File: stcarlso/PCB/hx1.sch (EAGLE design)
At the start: 5 parts, among them J1 SMA_EDGE, J2 CTRL, U1 HX1

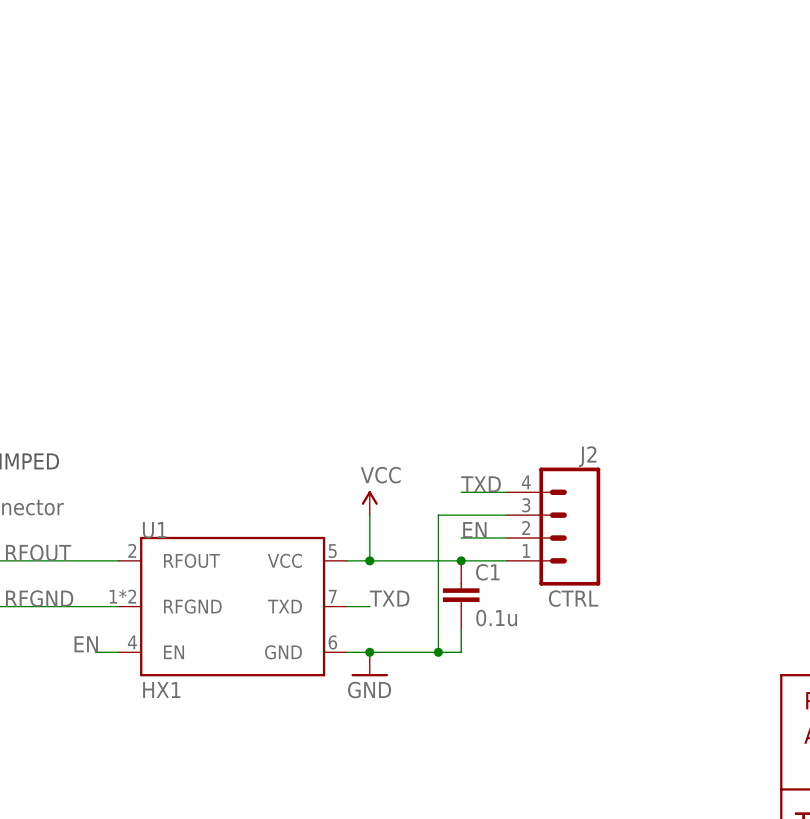
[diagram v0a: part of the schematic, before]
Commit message: Update PCB to include pads for RC filter (values TBD)
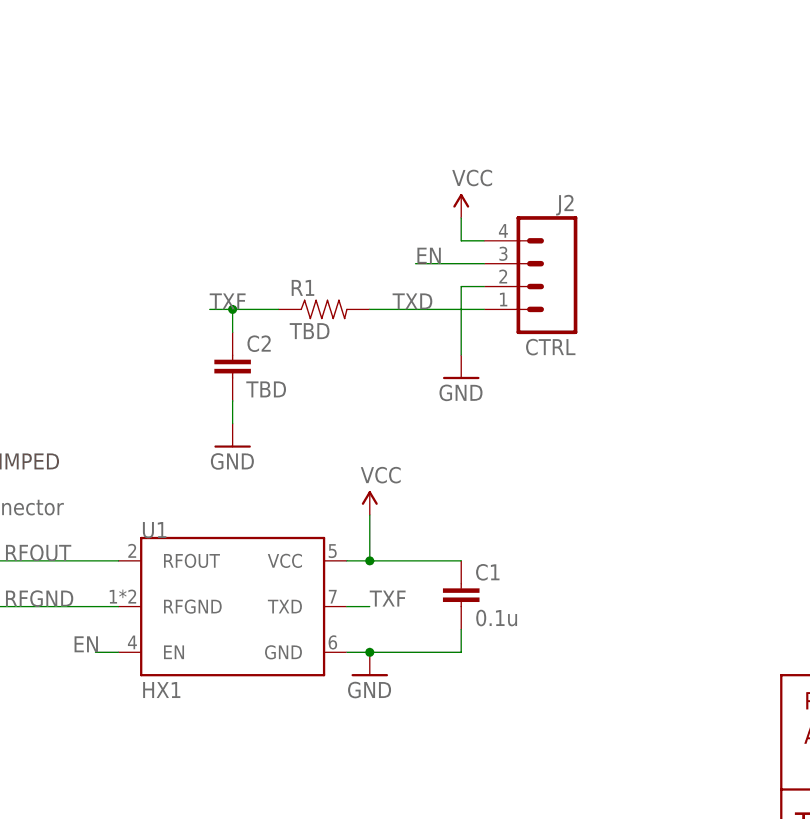
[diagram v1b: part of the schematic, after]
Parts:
- added C2: TBD, SparkFun-Passives:CAPPTH
- added R1: TBD, SparkFun-Passives:RESISTORAXIAL-0.3
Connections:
- new net TXF: C2.1, R1.1, U1.TXD
- net EN: now also J2.3; no longer J2.2
- net GND: now also C2.2, J2.2; no longer J2.3
- net TXD: now also J2.1, R1.2; no longer J2.4, U1.TXD
- net VCC: now also J2.4; no longer J2.1
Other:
- moved on the sheet: J2
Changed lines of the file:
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@@
 <part name="SUPPLY1" library="SparkFun-Aesthetics" deviceset="VCC" device=""/>
 <part name="C1" library="SparkFun-Passives" deviceset="CAP" device="PTH" value="0.1u"/>
+<part name="R1" library="SparkFun-Passives" deviceset="RESISTOR" device="AXIAL-0.3" value="TBD"/>
+<part name="C2" library="SparkFun-Passives" deviceset="CAP" device="PTH" value="TBD"/>
+<part name="GND2" library="SparkFun-Aesthetics" deviceset="GND" device=""/>
+<part name="GND3" library="SparkFun-Aesthetics" deviceset="GND" device=""/>
+<part name="SUPPLY2" library="SparkFun-Aesthetics" deviceset="VCC" device=""/>
 </parts>
 <sheets>
@@
 <instance part="FRAME1" gate="G$1" x="0" y="0"/>
 <instance part="FRAME1" gate="V" x="147.32" y="0"/>
-<instance part="J2" gate="G$1" x="121.92" y="50.8" rot="MR0"/>
+<instance part="J2" gate="G$1" x="119.38" y="78.74" rot="MR0"/>
 <instance part="GND1" gate="1" x="101.6" y="35.56"/>
 <instance part="SUPPLY1" gate="G$1" x="101.6" y="53.34"/>
 <instance part="C1" gate="G$1" x="111.76" y="43.18"/>
+<instance part="R1" gate="G$1" x="96.52" y="76.2"/>
+<instance part="C2" gate="G$1" x="86.36" y="68.58"/>
+<instance part="GND2" gate="1" x="86.36" y="60.96"/>
+<instance part="GND3" gate="1" x="111.76" y="68.58"/>
+<instance part="SUPPLY2" gate="G$1" x="111.76" y="86.36"/>
 </instances>
 <busses>
@@
 </segment>
 <segment>
-<pinref part="J2" gate="G$1" pin="2"/>
-<wire x1="111.76" y1="50.8" x2="116.84" y2="50.8" width="0.1524" layer="91"/>
-<label x="111.76" y="50.8" size="1.778" layer="95"/>
+<pinref part="J2" gate="G$1" pin="3"/>
+<wire x1="114.3" y1="81.28" x2="106.68" y2="81.28" width="0.1524" layer="91"/>
+<label x="106.68" y="81.28" size="1.778" layer="95"/>
 </segment>
 </net>
@@
 <wire x1="101.6" y1="48.26" x2="99.06" y2="48.26" width="0.1524" layer="91"/>
 <wire x1="101.6" y1="53.34" x2="101.6" y2="48.26" width="0.1524" layer="91"/>
-<pinref part="J2" gate="G$1" pin="1"/>
 <wire x1="101.6" y1="48.26" x2="111.76" y2="48.26" width="0.1524" layer="91"/>
 <junction x="101.6" y="48.26"/>
 <pinref part="C1" gate="G$1" pin="1"/>
-<wire x1="111.76" y1="48.26" x2="116.84" y2="48.26" width="0.1524" layer="91"/>
-<junction x="111.76" y="48.26"/>
-</segment>
-</net>
-<net name="TXD" class="0">
-<segment>
-<pinref part="U1" gate="G$1" pin="TXD"/>
-<wire x1="101.6" y1="43.18" x2="99.06" y2="43.18" width="0.1524" layer="91"/>
-<label x="101.6" y="43.18" size="1.778" layer="95"/>
 </segment>
 <segment>
 <pinref part="J2" gate="G$1" pin="4"/>
-<wire x1="111.76" y1="55.88" x2="116.84" y2="55.88" width="0.1524" layer="91"/>
-<label x="111.76" y="55.88" size="1.778" layer="95"/>
+<pinref part="SUPPLY2" gate="G$1" pin="VCC"/>
+<wire x1="114.3" y1="83.82" x2="111.76" y2="83.82" width="0.1524" layer="91"/>
+<wire x1="111.76" y1="83.82" x2="111.76" y2="86.36" width="0.1524" layer="91"/>
 </segment>
 </net>
@@
 <wire x1="101.6" y1="38.1" x2="99.06" y2="38.1" width="0.1524" layer="91"/>
 <pinref part="GND1" gate="1" pin="GND"/>
-<pinref part="J2" gate="G$1" pin="3"/>
-<wire x1="109.22" y1="53.34" x2="116.84" y2="53.34" width="0.1524" layer="91"/>
-<wire x1="109.22" y1="53.34" x2="109.22" y2="38.1" width="0.1524" layer="91"/>
-<wire x1="101.6" y1="38.1" x2="109.22" y2="38.1" width="0.1524" layer="91"/>
+<wire x1="101.6" y1="38.1" x2="111.76" y2="38.1" width="0.1524" layer="91"/>
 <junction x="101.6" y="38.1"/>
 <pinref part="C1" gate="G$1" pin="2"/>
 <wire x1="111.76" y1="40.64" x2="111.76" y2="38.1" width="0.1524" layer="91"/>
-<wire x1="111.76" y1="38.1" x2="109.22" y2="38.1" width="0.1524" layer="91"/>
-<junction x="109.22" y="38.1"/>
+</segment>
+<segment>
+<pinref part="C2" gate="G$1" pin="2"/>
+<pinref part="GND2" gate="1" pin="GND"/>
+<wire x1="86.36" y1="66.04" x2="86.36" y2="63.5" width="0.1524" layer="91"/>
+</segment>
+<segment>
+<pinref part="J2" gate="G$1" pin="2"/>
+<pinref part="GND3" gate="1" pin="GND"/>
+<wire x1="114.3" y1="78.74" x2="111.76" y2="78.74" width="0.1524" layer="91"/>
+<wire x1="111.76" y1="78.74" x2="111.76" y2="71.12" width="0.1524" layer="91"/>
 </segment>
 </net>
+<net name="TXF" class="0">
+<segment>
+<pinref part="R1" gate="G$1" pin="1"/>
+<pinref part="C2" gate="G$1" pin="1"/>
+<wire x1="91.44" y1="76.2" x2="86.36" y2="76.2" width="0.1524" layer="91"/>
+<wire x1="86.36" y1="76.2" x2="86.36" y2="73.66" width="0.1524" layer="91"/>
+<wire x1="83.82" y1="76.2" x2="86.36" y2="76.2" width="0.1524" layer="91"/>
+<junction x="86.36" y="76.2"/>
+<label x="83.82" y="76.2" size="1.778" layer="95"/>
+</segment>
+<segment>
+<pinref part="U1" gate="G$1" pin="TXD"/>
+<wire x1="101.6" y1="43.18" x2="99.06" y2="43.18" width="0.1524" layer="91"/>
+<label x="101.6" y="43.18" size="1.778" layer="95"/>
+</segment>
+</net>
+<net name="TXD" class="0">
+<segment>
+<pinref part="R1" gate="G$1" pin="2"/>
+<pinref part="J2" gate="G$1" pin="1"/>
+<wire x1="101.6" y1="76.2" x2="114.3" y2="76.2" width="0.1524" layer="91"/>
+<label x="104.14" y="76.2" size="1.778" layer="95"/>
+</segment>
+</net>
